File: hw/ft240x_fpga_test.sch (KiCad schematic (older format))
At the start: 0 parts

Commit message: several updates...
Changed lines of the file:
@@
 $Descr A4 11693 8268
 encoding utf-8
-Sheet 1 4
+Sheet 1 5
 Title ""
 Date ""
@@
 F1 "pll_clock.sch" 50
 $EndSheet
+$Sheet
+S 5250 4750 1450 1300
+U 612B1274
+F0 "ADC+Driver" 50
+F1 "max19507.sch" 50
+$EndSheet
 $EndSCHEMATC

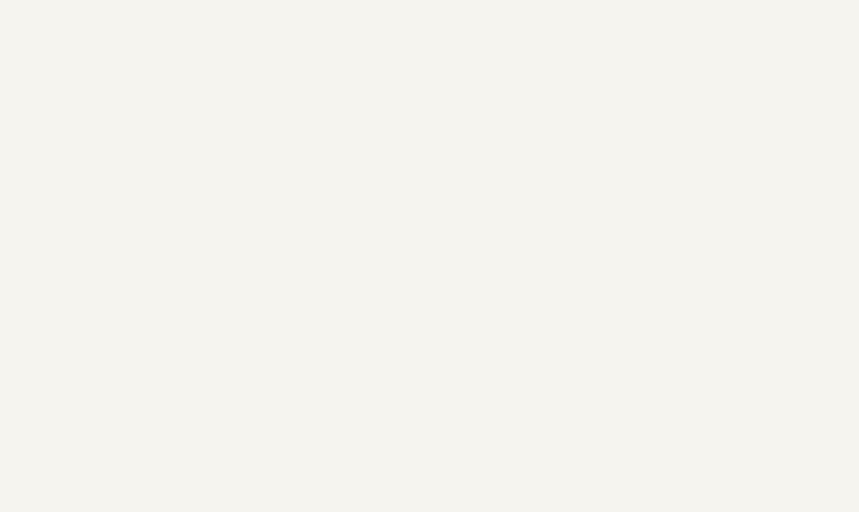
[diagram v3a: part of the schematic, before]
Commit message: everything hooked up + layed out; 0.2/0.4mm vias :-(
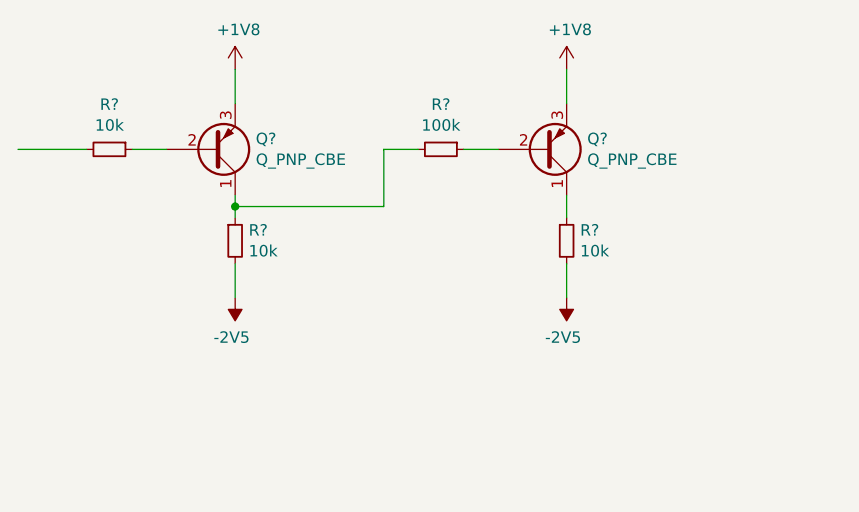
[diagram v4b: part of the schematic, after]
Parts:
- added Q? (x2): Q_PNP_CBE, symbol Device:Q_PNP_CBE
- added R? (x3): 10k, symbol Device:R_Small
- added R?: 100k, symbol Device:R_Small
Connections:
- net labels added: +1V8, -2V5
- wire segments 0 -> 13
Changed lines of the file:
@@
 $Descr A4 11693 8268
 encoding utf-8
-Sheet 1 8
+Sheet 1 9
 Title ""
 Date ""
@@
 F1 "max19507.sch" 50
 $EndSheet
+$Comp
+L Device:Q_PNP_CBE Q?
+U 1 1 60F1B962
+P 2050 2650
+F 0 "Q?" H 2240 2604 50  0000 L CNN
+F 1 "Q_PNP_CBE" H 2240 2695 50  0000 L CNN
+F 2 "" H 2250 2750 50  0001 C CNN
+F 3 "~" H 2050 2650 50  0001 C CNN
+	1    2050 2650
+	1    0    0    1
+$EndComp
+$Comp
+L power:+1V8 #PWR?
+U 1 1 60F30A19
+P 2150 2300
+AR Path="/6086F2E3/60F30A19" Ref="#PWR?"  Part="1"
+AR Path="/60AABC24/60F30A19" Ref="#PWR?"  Part="1"
+AR Path="/60F30A19" Ref="#PWR?"  Part="1"
+F 0 "#PWR?" H 2150 2150 50  0001 C CNN
+F 1 "+1V8" H 2165 2473 50  0000 C CNN
+F 2 "" H 2150 2300 50  0001 C CNN
+F 3 "" H 2150 2300 50  0001 C CNN
+	1    2150 2300
+	1    0    0    -1
+$EndComp
+$Comp
+L power:-2V5 #PWR?
+U 1 1 60F43801
+P 2150 3300
+F 0 "#PWR?" H 2150 3400 50  0001 C CNN
+F 1 "-2V5" H 2165 3473 50  0000 C CNN
+F 2 "" H 2150 3300 50  0001 C CNN
+F 3 "" H 2150 3300 50  0001 C CNN
+	1    2150 3300
+	-1   0    0    1
+$EndComp
+$Comp
+L Device:R_Small R?
+U 1 1 60F43AB9
+P 2150 3050
+F 0 "R?" H 2209 3096 50  0000 L CNN
+F 1 "10k" H 2209 3005 50  0000 L CNN
+F 2 "" H 2150 3050 50  0001 C CNN
+F 3 "~" H 2150 3050 50  0001 C CNN
+	1    2150 3050
+	1    0    0    -1
+$EndComp
+Wire Wire Line
+	2150 2300 2150 2450
+Wire Wire Line
+	2150 2850 2150 2900
+Wire Wire Line
+	2150 3150 2150 3300
+$Comp
+L Device:R_Small R?
+U 1 1 60F442F1
+P 1600 2650
+F 0 "R?" V 1404 2650 50  0000 C CNN
+F 1 "10k" V 1495 2650 50  0000 C CNN
+F 2 "" H 1600 2650 50  0001 C CNN
+F 3 "~" H 1600 2650 50  0001 C CNN
+	1    1600 2650
+	0    1    1    0
+$EndComp
+Wire Wire Line
+	1700 2650 1850 2650
+$Comp
+L Device:Q_PNP_CBE Q?
+U 1 1 60F44D1B
+P 3500 2650
+F 0 "Q?" H 3690 2604 50  0000 L CNN
+F 1 "Q_PNP_CBE" H 3690 2695 50  0000 L CNN
+F 2 "" H 3700 2750 50  0001 C CNN
+F 3 "~" H 3500 2650 50  0001 C CNN
+	1    3500 2650
+	1    0    0    1
+$EndComp
+$Comp
+L power:+1V8 #PWR?
+U 1 1 60F44D91
+P 3600 2300
+AR Path="/6086F2E3/60F44D91" Ref="#PWR?"  Part="1"
+AR Path="/60AABC24/60F44D91" Ref="#PWR?"  Part="1"
+AR Path="/60F44D91" Ref="#PWR?"  Part="1"
+F 0 "#PWR?" H 3600 2150 50  0001 C CNN
+F 1 "+1V8" H 3615 2473 50  0000 C CNN
+F 2 "" H 3600 2300 50  0001 C CNN
+F 3 "" H 3600 2300 50  0001 C CNN
+	1    3600 2300
+	1    0    0    -1
+$EndComp
+$Comp
+L power:-2V5 #PWR?
+U 1 1 60F44D9B
+P 3600 3300
+F 0 "#PWR?" H 3600 3400 50  0001 C CNN
+F 1 "-2V5" H 3615 3473 50  0000 C CNN
+F 2 "" H 3600 3300 50  0001 C CNN
+F 3 "" H 3600 3300 50  0001 C CNN
+	1    3600 3300
+	-1   0    0    1
+$EndComp
+$Comp
+L Device:R_Small R?
+U 1 1 60F44DA5
+P 3600 3050
+F 0 "R?" H 3659 3096 50  0000 L CNN
+F 1 "10k" H 3659 3005 50  0000 L CNN
+F 2 "" H 3600 3050 50  0001 C CNN
+F 3 "~" H 3600 3050 50  0001 C CNN
+	1    3600 3050
+	1    0    0    -1
+$EndComp
+Wire Wire Line
+	3600 2300 3600 2450
+Wire Wire Line
+	3600 2850 3600 2950
+Wire Wire Line
+	3600 3150 3600 3300
+$Comp
+L Device:R_Small R?
+U 1 1 60F44DB2
+P 3050 2650
+F 0 "R?" V 2854 2650 50  0000 C CNN
+F 1 "100k" V 2945 2650 50  0000 C CNN
+F 2 "" H 3050 2650 50  0001 C CNN
+F 3 "~" H 3050 2650 50  0001 C CNN
+	1    3050 2650
+	0    1    1    0
+$EndComp
+Wire Wire Line
+	3150 2650 3300 2650
+Wire Wire Line
+	2150 2900 2800 2900
+Wire Wire Line
+	2800 2900 2800 2650
+Wire Wire Line
+	2800 2650 2950 2650
+Connection ~ 2150 2900
+Wire Wire Line
+	2150 2900 2150 2950
+Wire Wire Line
+	1500 2650 1200 2650
 $EndSCHEMATC

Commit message: prototype version
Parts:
- removed Q? (x2): Q_PNP_CBE, symbol Device:Q_PNP_CBE
- removed R? (x3): 10k, symbol Device:R_Small
- removed R?: 100k, symbol Device:R_Small
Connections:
- net labels removed: +1V8, -2V5
- wire segments 13 -> 0
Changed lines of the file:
@@
 F1 "max19507.sch" 50
 $EndSheet
-$Comp
-L Device:Q_PNP_CBE Q?
-U 1 1 60F1B962
-P 2050 2650
-F 0 "Q?" H 2240 2604 50  0000 L CNN
-F 1 "Q_PNP_CBE" H 2240 2695 50  0000 L CNN
-F 2 "" H 2250 2750 50  0001 C CNN
-F 3 "~" H 2050 2650 50  0001 C CNN
-	1    2050 2650
-	1    0    0    1
-$EndComp
-$Comp
-L power:+1V8 #PWR?
-U 1 1 60F30A19
-P 2150 2300
-AR Path="/6086F2E3/60F30A19" Ref="#PWR?"  Part="1"
-AR Path="/60AABC24/60F30A19" Ref="#PWR?"  Part="1"
-AR Path="/60F30A19" Ref="#PWR?"  Part="1"
-F 0 "#PWR?" H 2150 2150 50  0001 C CNN
-F 1 "+1V8" H 2165 2473 50  0000 C CNN
-F 2 "" H 2150 2300 50  0001 C CNN
-F 3 "" H 2150 2300 50  0001 C CNN
-	1    2150 2300
-	1    0    0    -1
-$EndComp
-$Comp
-L power:-2V5 #PWR?
-U 1 1 60F43801
-P 2150 3300
-F 0 "#PWR?" H 2150 3400 50  0001 C CNN
-F 1 "-2V5" H 2165 3473 50  0000 C CNN
-F 2 "" H 2150 3300 50  0001 C CNN
-F 3 "" H 2150 3300 50  0001 C CNN
-	1    2150 3300
-	-1   0    0    1
-$EndComp
-$Comp
-L Device:R_Small R?
-U 1 1 60F43AB9
-P 2150 3050
-F 0 "R?" H 2209 3096 50  0000 L CNN
-F 1 "10k" H 2209 3005 50  0000 L CNN
-F 2 "" H 2150 3050 50  0001 C CNN
-F 3 "~" H 2150 3050 50  0001 C CNN
-	1    2150 3050
-	1    0    0    -1
-$EndComp
-Wire Wire Line
-	2150 2300 2150 2450
-Wire Wire Line
-	2150 2850 2150 2900
-Wire Wire Line
-	2150 3150 2150 3300
-$Comp
-L Device:R_Small R?
-U 1 1 60F442F1
-P 1600 2650
-F 0 "R?" V 1404 2650 50  0000 C CNN
-F 1 "10k" V 1495 2650 50  0000 C CNN
-F 2 "" H 1600 2650 50  0001 C CNN
-F 3 "~" H 1600 2650 50  0001 C CNN
-	1    1600 2650
-	0    1    1    0
-$EndComp
-Wire Wire Line
-	1700 2650 1850 2650
-$Comp
-L Device:Q_PNP_CBE Q?
-U 1 1 60F44D1B
-P 3500 2650
-F 0 "Q?" H 3690 2604 50  0000 L CNN
-F 1 "Q_PNP_CBE" H 3690 2695 50  0000 L CNN
-F 2 "" H 3700 2750 50  0001 C CNN
-F 3 "~" H 3500 2650 50  0001 C CNN
-	1    3500 2650
-	1    0    0    1
-$EndComp
-$Comp
-L power:+1V8 #PWR?
-U 1 1 60F44D91
-P 3600 2300
-AR Path="/6086F2E3/60F44D91" Ref="#PWR?"  Part="1"
-AR Path="/60AABC24/60F44D91" Ref="#PWR?"  Part="1"
-AR Path="/60F44D91" Ref="#PWR?"  Part="1"
-F 0 "#PWR?" H 3600 2150 50  0001 C CNN
-F 1 "+1V8" H 3615 2473 50  0000 C CNN
-F 2 "" H 3600 2300 50  0001 C CNN
-F 3 "" H 3600 2300 50  0001 C CNN
-	1    3600 2300
-	1    0    0    -1
-$EndComp
-$Comp
-L power:-2V5 #PWR?
-U 1 1 60F44D9B
-P 3600 3300
-F 0 "#PWR?" H 3600 3400 50  0001 C CNN
-F 1 "-2V5" H 3615 3473 50  0000 C CNN
-F 2 "" H 3600 3300 50  0001 C CNN
-F 3 "" H 3600 3300 50  0001 C CNN
-	1    3600 3300
-	-1   0    0    1
-$EndComp
-$Comp
-L Device:R_Small R?
-U 1 1 60F44DA5
-P 3600 3050
-F 0 "R?" H 3659 3096 50  0000 L CNN
-F 1 "10k" H 3659 3005 50  0000 L CNN
-F 2 "" H 3600 3050 50  0001 C CNN
-F 3 "~" H 3600 3050 50  0001 C CNN
-	1    3600 3050
-	1    0    0    -1
-$EndComp
-Wire Wire Line
-	3600 2300 3600 2450
-Wire Wire Line
-	3600 2850 3600 2950
-Wire Wire Line
-	3600 3150 3600 3300
-$Comp
-L Device:R_Small R?
-U 1 1 60F44DB2
-P 3050 2650
-F 0 "R?" V 2854 2650 50  0000 C CNN
-F 1 "100k" V 2945 2650 50  0000 C CNN
-F 2 "" H 3050 2650 50  0001 C CNN
-F 3 "~" H 3050 2650 50  0001 C CNN
-	1    3050 2650
-	0    1    1    0
-$EndComp
-Wire Wire Line
-	3150 2650 3300 2650
-Wire Wire Line
-	2150 2900 2800 2900
-Wire Wire Line
-	2800 2900 2800 2650
-Wire Wire Line
-	2800 2650 2950 2650
-Connection ~ 2150 2900
-Wire Wire Line
-	2150 2900 2150 2950
-Wire Wire Line
-	1500 2650 1200 2650
 $EndSCHEMATC
